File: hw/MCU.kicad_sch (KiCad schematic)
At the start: 14 parts, among them J2 Conn_01x06, SW2 SKRPACE010, SW3 SKRPACE010, U2 N32L406RBL7

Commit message: updated Designs
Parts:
- added C14: 100n, Capacitor_SMD:C_0805_2012Metric_Pad1.18x1.45mm_HandSolder, symbol Device:C
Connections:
- net GND: now also C14.2
- net VDD: now also C14.1
- net HighSide_Row_9: now reaches U2.2 (PC13)
- net HighSide_Row_10: now reaches U2.3 (PC14)
- net HighSide_Row_11: now reaches U2.4 (PC15)
- net HighSide_Row_12: now reaches U2.5 (PD14)
- net HighSide_Input_Row_1 renamed HighSide_Row_1
- net HighSide_Input_Row_2 renamed HighSide_Row_2
- net HighSide_Input_Row_3 renamed HighSide_Row_3
- net HighSide_Input_Row_4 renamed HighSide_Row_4
- net HighSide_Input_Row_5 renamed HighSide_Row_5
- net HighSide_Input_Row_6 renamed HighSide_Row_6
- net HighSide_Input_Row_7 renamed HighSide_Row_7
- net HighSide_Input_Row_8 renamed HighSide_Row_8
- net LowSide_Input_B_Col_1 renamed LowSide_B_Col_1
- net LowSide_Input_B_Col_2 renamed LowSide_B_Col_2
- net LowSide_Input_B_Col_3 renamed LowSide_B_Col_3
- net LowSide_Input_B_Col_4 renamed LowSide_B_Col_4
- net LowSide_Input_B_Col_5 renamed LowSide_B_Col_5
- net LowSide_Input_B_Col_6 renamed LowSide_B_Col_6
- net LowSide_Input_G_Col_1 renamed LowSide_R_Col_2
- net LowSide_Input_G_Col_2 renamed LowSide_G_Col_1
- net LowSide_Input_G_Col_3 renamed LowSide_G_Col_3
- net LowSide_Input_G_Col_4 renamed LowSide_G_Col_4
- net LowSide_Input_G_Col_5 renamed LowSide_G_Col_2
- net LowSide_Input_G_Col_6 renamed LowSide_G_Col_6
- net LowSide_Input_R_Col_1 renamed LowSide_G_Col_5
- net LowSide_Input_R_Col_2 renamed LowSide_R_Col_1
- net LowSide_Input_R_Col_3 renamed LowSide_R_Col_3
- net LowSide_Input_R_Col_4 renamed LowSide_R_Col_4
- net LowSide_Input_R_Col_5 renamed LowSide_R_Col_5
- net LowSide_Input_R_Col_6 renamed LowSide_R_Col_6
- no-connect marks 7 -> 3
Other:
- moved on the sheet: C5, C6, C7, C8

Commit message: routed some row control lines
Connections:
- net LowSide_B_Col_4 is gone; now on net HighSide_Row_6: U2.15 (PA1)
- net LowSide_G_Col_2 is gone; now on net HighSide_Row_3: U2.17 (PA3)
- net LowSide_G_Col_4 is gone; now on net HighSide_Row_9: U2.14 (PA0)
- net LowSide_R_Col_5 is gone; now on net HighSide_Row_4: U2.16 (PA2)
- net HighSide_Row_3: no longer U2.53 (PC12)
- net HighSide_Row_4: no longer U2.54 (PD2)
- net HighSide_Row_6: no longer U2.9 (PC1)
- net HighSide_Row_9: no longer U2.2 (PC13)
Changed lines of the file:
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@@
-    (stroke (width 0) (type default))
-  )
-  (wire (pts (xy 43.18 97.79) (xy 53.34 97.79))
     (stroke (width 0) (type default))
   )
@@
     (stroke (width 0) (type default))
   )
-  (wire (pts (xy 43.18 77.47) (xy 53.34 77.47))
-    (stroke (width 0) (type default))
-  )
   (wire (pts (xy 43.18 58.42) (xy 53.34 58.42))
     (stroke (width 0) (type default))
@@
     (stroke (width 0) (type default))
   )
-  (wire (pts (xy 43.18 105.41) (xy 53.34 105.41))
-    (stroke (width 0) (type default))
-  )
   (wire (pts (xy 168.91 30.48) (xy 168.91 33.02))
     (stroke (width 0) (type default))
@@
   )
   (wire (pts (xy 238.76 88.9) (xy 254 88.9))
-    (stroke (width 0) (type default))
-  )
-  (wire (pts (xy 43.18 100.33) (xy 53.34 100.33))
     (stroke (width 0) (type default))
   )
@@
     (effects (font (size 1.27 1.27)) (justify right bottom))
   )
-  (label "HighSide_Row_9" (at 114.3 81.28 180) (fields_autoplaced)
-    (effects (font (size 1.27 1.27)) (justify right bottom))
-  )
-  (label "LowSide_R_Col_5" (at 114.3 114.3 180) (fields_autoplaced)
+  (label "HighSide_Row_9" (at 114.3 109.22 180) (fields_autoplaced)
     (effects (font (size 1.27 1.27)) (justify right bottom))
   )
@@
     (effects (font (size 1.27 1.27)) (justify right bottom))
   )
-  (label "LowSide_G_Col_4" (at 53.34 97.79 0) (fields_autoplaced)
-    (effects (font (size 1.27 1.27)) (justify left bottom))
-  )
   (label "IMU_INT2" (at 53.34 175.26 0) (fields_autoplaced)
     (effects (font (size 1.27 1.27)) (justify left bottom))
@@
     (effects (font (size 1.27 1.27)) (justify left bottom))
   )
-  (label "LowSide_B_Col_4" (at 53.34 100.33 0) (fields_autoplaced)
-    (effects (font (size 1.27 1.27)) (justify left bottom))
-  )
   (label "HighSide_Row_7" (at 53.34 45.72 0) (fields_autoplaced)
     (effects (font (size 1.27 1.27)) (justify left bottom))
@@
     (effects (font (size 1.27 1.27)) (justify right bottom))
   )
-  (label "LowSide_G_Col_4" (at 114.3 109.22 180) (fields_autoplaced)
-    (effects (font (size 1.27 1.27)) (justify right bottom))
-  )
   (label "LowSide_B_Col_2" (at 160.02 137.16 270) (fields_autoplaced)
     (effects (font (size 1.27 1.27)) (justify right bottom))
@@
     (effects (font (size 1.27 1.27)) (justify right bottom))
   )
-  (label "LowSide_G_Col_2" (at 53.34 77.47 0) (fields_autoplaced)
-    (effects (font (size 1.27 1.27)) (justify left bottom))
-  )
   (label "LowSide_R_Col_1" (at 53.34 64.77 0) (fields_autoplaced)
     (effects (font (size 1.27 1.27)) (justify left bottom))
@@
     (effects (font (size 1.27 1.27)) (justify left bottom))
   )
-  (label "LowSide_R_Col_5" (at 53.34 105.41 0) (fields_autoplaced)
-    (effects (font (size 1.27 1.27)) (justify left bottom))
-  )
   (label "HighSide_Row_11" (at 114.3 86.36 180) (fields_autoplaced)
     (effects (font (size 1.27 1.27)) (justify right bottom))
@@
     (effects (font (size 1.27 1.27)) (justify left bottom))
   )
-  (label "LowSide_G_Col_2" (at 137.16 137.16 270) (fields_autoplaced)
-    (effects (font (size 1.27 1.27)) (justify right bottom))
-  )
   (label "VDDA" (at 175.26 137.16 270) (fields_autoplaced)
     (effects (font (size 1.27 1.27)) (justify right bottom))
@@
     (effects (font (size 1.27 1.27)) (justify right bottom))
   )
-  (label "HighSide_Row_3" (at 162.56 60.96 90) (fields_autoplaced)
-    (effects (font (size 1.27 1.27)) (justify left bottom))
+  (label "HighSide_Row_3" (at 137.16 137.16 270) (fields_autoplaced)
+    (effects (font (size 1.27 1.27)) (justify right bottom))
   )
   (label "LowSide_G_Col_6" (at 53.34 118.11 0) (fields_autoplaced)
     (effects (font (size 1.27 1.27)) (justify left bottom))
   )
-  (label "HighSide_Row_6" (at 114.3 99.06 180) (fields_autoplaced)
+  (label "HighSide_Row_6" (at 114.3 111.76 180) (fields_autoplaced)
     (effects (font (size 1.27 1.27)) (justify right bottom))
   )
@@
     (effects (font (size 1.27 1.27)) (justify left bottom))
   )
-  (label "HighSide_Row_4" (at 160.02 60.96 90) (fields_autoplaced)
-    (effects (font (size 1.27 1.27)) (justify left bottom))
+  (label "HighSide_Row_4" (at 114.3 114.3 180) (fields_autoplaced)
+    (effects (font (size 1.27 1.27)) (justify right bottom))
   )
   (label "IMU_INT2" (at 162.56 137.16 270) (fields_autoplaced)
@@
     (effects (font (size 1.27 1.27)) (justify left bottom))
   )
-  (label "LowSide_B_Col_4" (at 114.3 111.76 180) (fields_autoplaced)
-    (effects (font (size 1.27 1.27)) (justify right bottom))
-  )
   (label "LowSide_B_Col_2" (at 53.34 80.01 0) (fields_autoplaced)
     (effects (font (size 1.27 1.27)) (justify left bottom))
@@
     (effects (font (size 1.27 1.27)) (justify right))
   )
-  (hierarchical_label "LowSide_G_Col_2" (shape output) (at 43.18 77.47 180) (fields_autoplaced)
-    (effects (font (size 1.27 1.27)) (justify right))
-  )
   (hierarchical_label "IMU_MISO" (shape input) (at 43.18 165.1 180) (fields_autoplaced)
     (effects (font (size 1.27 1.27)) (justify right))
@@
     (effects (font (size 1.27 1.27)) (justify right))
   )
-  (hierarchical_label "LowSide_B_Col_4" (shape output) (at 43.18 100.33 180) (fields_autoplaced)
-    (effects (font (size 1.27 1.27)) (justify right))
-  )
   (hierarchical_label "SAO_1_GPIO2" (shape output) (at 43.18 153.67 180) (fields_autoplaced)
     (effects (font (size 1.27 1.27)) (justify right))
   )
-  (hierarchical_label "LowSide_G_Col_4" (shape output) (at 43.18 97.79 180) (fields_autoplaced)
-    (effects (font (size 1.27 1.27)) (justify right))
-  )
   (hierarchical_label "LowSide_R_Col_4" (shape output) (at 43.18 95.25 180) (fields_autoplaced)
-    (effects (font (size 1.27 1.27)) (justify right))
-  )
-  (hierarchical_label "LowSide_R_Col_5" (shape output) (at 43.18 105.41 180) (fields_autoplaced)
     (effects (font (size 1.27 1.27)) (justify right))
   )
@@
     (pin "12")
     (pin "13")
-    (pin "14" (alternate "TIM5_CH1"))
-    (pin "15" (alternate "TIM5_CH2"))
-    (pin "16" (alternate "TIM5_CH3"))
-    (pin "17" (alternate "TIM5_CH4"))
+    (pin "14")
+    (pin "15")
+    (pin "16")
+    (pin "17")
     (pin "18")
     (pin "19")

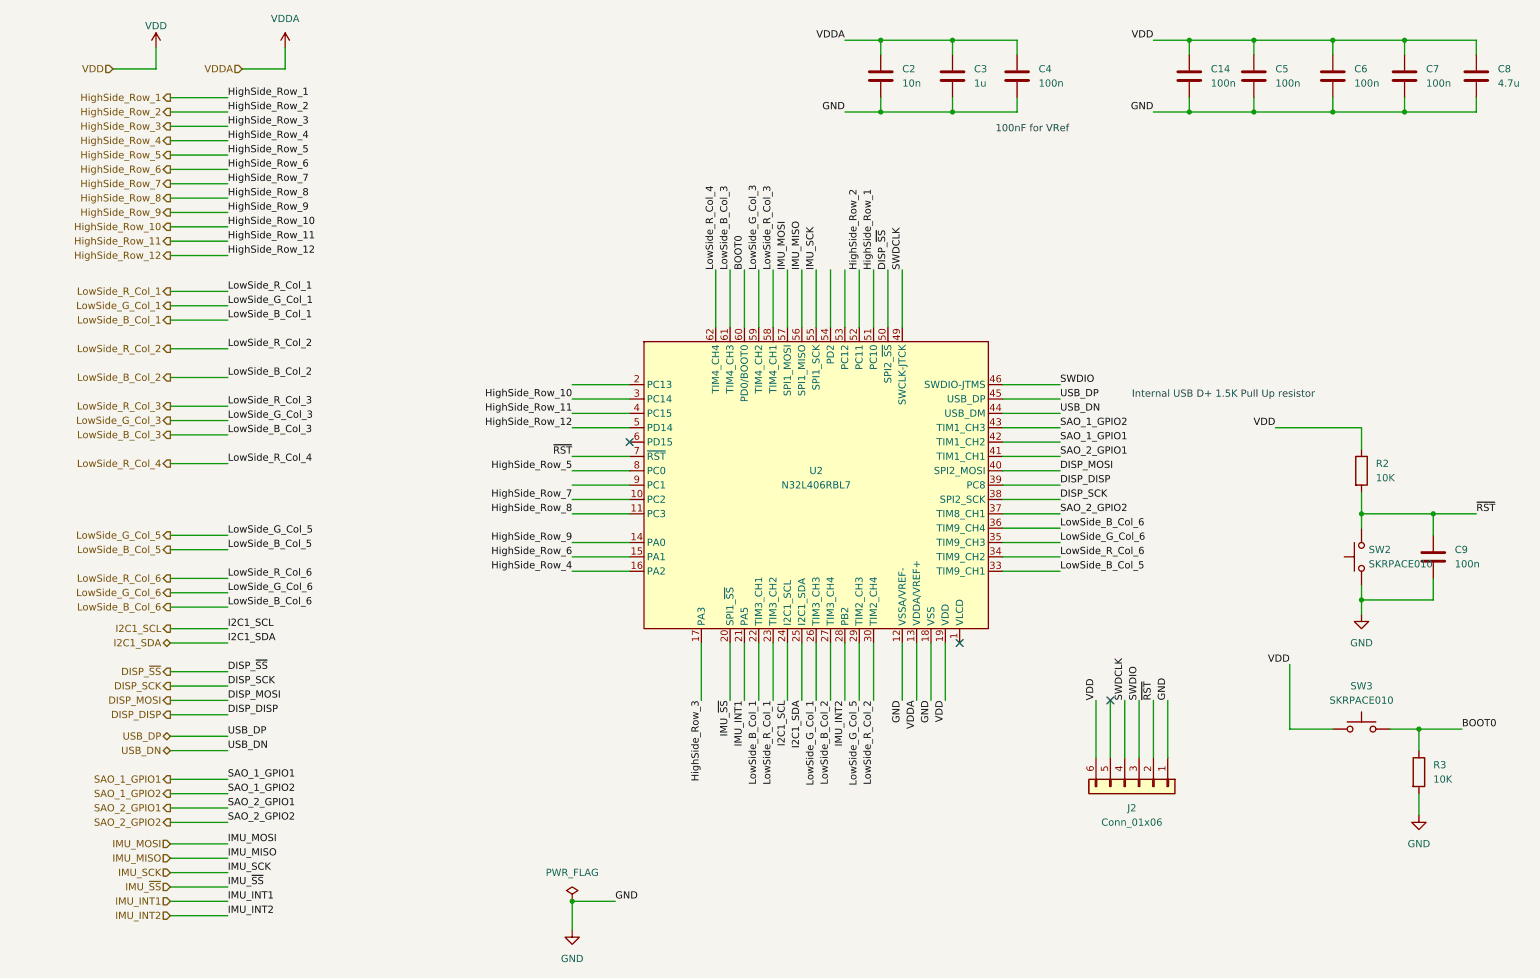
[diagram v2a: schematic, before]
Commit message: routed HighSide MOS
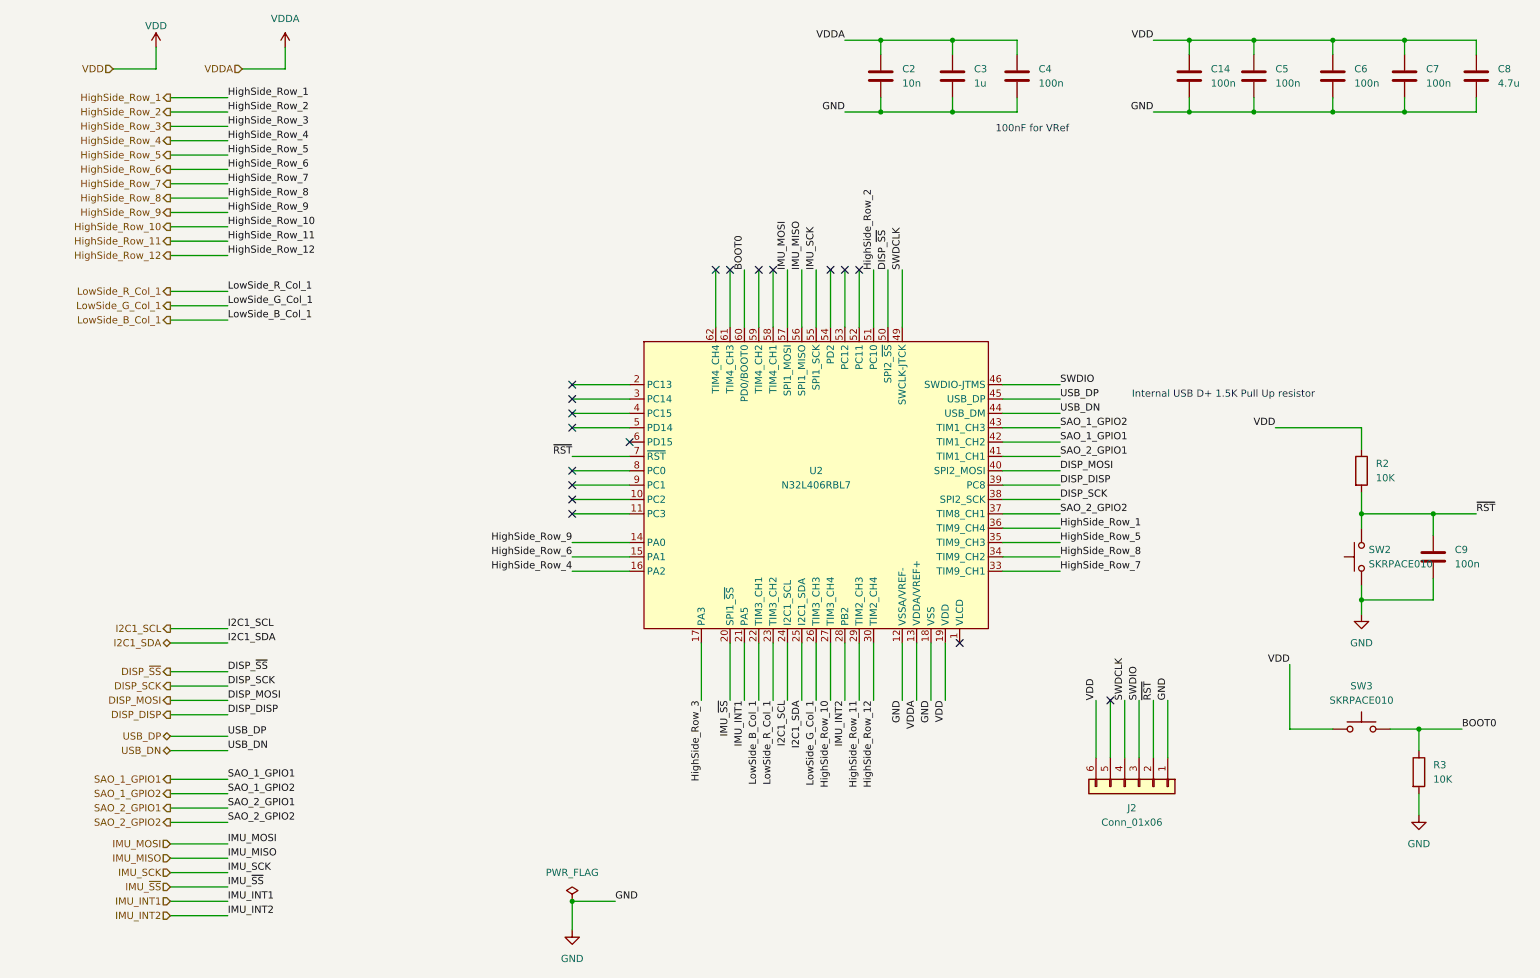
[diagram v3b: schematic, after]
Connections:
- net LowSide_B_Col_2 is gone; now on net HighSide_Row_10: U2.27 (PB1)
- net LowSide_B_Col_5 is gone; now on net HighSide_Row_7: U2.33 (PB12)
- net LowSide_B_Col_6 is gone; now on net HighSide_Row_1: U2.36 (PB15)
- net LowSide_G_Col_5 is gone; now on net HighSide_Row_11: U2.29 (PB10)
- net LowSide_G_Col_6 is gone; now on net HighSide_Row_5: U2.35 (PB14)
- net LowSide_R_Col_2 is gone; now on net HighSide_Row_12: U2.30 (PB11)
- net LowSide_R_Col_6 is gone; now on net HighSide_Row_8: U2.34 (PB13)
- net HighSide_Row_1: no longer U2.51 (PC10)
- net HighSide_Row_10: no longer U2.3 (PC14)
- net HighSide_Row_11: no longer U2.4 (PC15)
- net HighSide_Row_12: no longer U2.5 (PD14)
- net HighSide_Row_2: now also U2.51 (PC10); no longer U2.52 (PC11)
- net HighSide_Row_5: no longer U2.8 (PC0)
- net HighSide_Row_7: no longer U2.10 (PC2)
- net HighSide_Row_8: no longer U2.11 (PC3)
- net LowSide_B_Col_3: no longer names the net of U2.61 (PB8)
- net LowSide_G_Col_3: no longer names the net of U2.59 (PB7)
- net LowSide_R_Col_3: no longer names the net of U2.58 (PB6)
- net LowSide_R_Col_4: no longer names the net of U2.62 (PB9)
- no-connect marks 3 -> 18

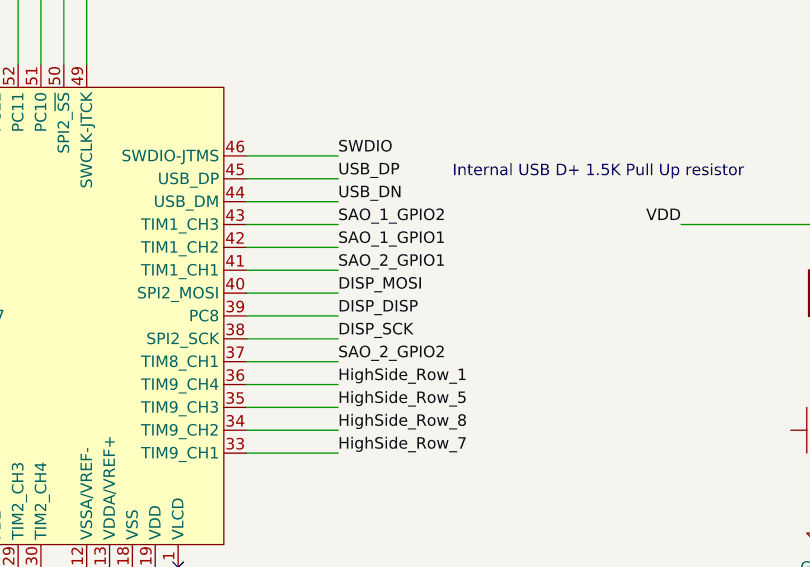
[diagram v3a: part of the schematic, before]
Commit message: routed SAO GPIO
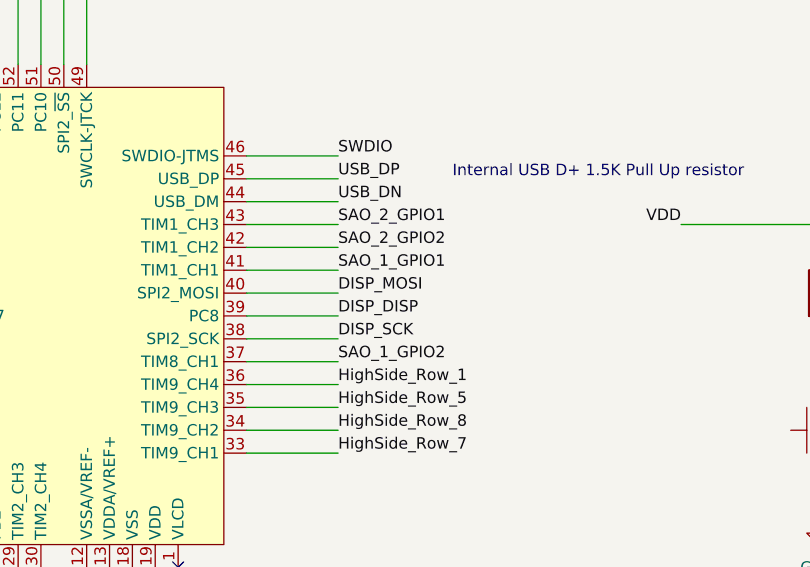
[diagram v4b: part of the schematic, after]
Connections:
- net SAO_1_GPIO1: now also U2.41 (PA8); no longer U2.42 (PA9)
- net SAO_1_GPIO2: now also U2.37 (PC6); no longer U2.43 (PA10)
- net SAO_2_GPIO1: now also U2.43 (PA10); no longer U2.41 (PA8)
- net SAO_2_GPIO2: now also U2.42 (PA9); no longer U2.37 (PC6)
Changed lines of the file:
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@@
     (effects (font (size 1.27 1.27)) (justify left bottom))
   )
-  (label "SAO_2_GPIO2" (at 200.66 104.14 0) (fields_autoplaced)
+  (label "SAO_2_GPIO2" (at 200.66 91.44 0) (fields_autoplaced)
     (effects (font (size 1.27 1.27)) (justify left bottom))
   )
@@
     (effects (font (size 1.27 1.27)) (justify right bottom))
   )
-  (label "SAO_2_GPIO1" (at 200.66 93.98 0) (fields_autoplaced)
+  (label "SAO_2_GPIO1" (at 200.66 88.9 0) (fields_autoplaced)
     (effects (font (size 1.27 1.27)) (justify left bottom))
   )
@@
     (effects (font (size 1.27 1.27)) (justify left bottom))
   )
-  (label "SAO_1_GPIO2" (at 200.66 88.9 0) (fields_autoplaced)
+  (label "SAO_1_GPIO2" (at 200.66 104.14 0) (fields_autoplaced)
     (effects (font (size 1.27 1.27)) (justify left bottom))
   )
@@
     (effects (font (size 1.27 1.27)) (justify left bottom))
   )
-  (label "SAO_1_GPIO1" (at 200.66 91.44 0) (fields_autoplaced)
+  (label "SAO_1_GPIO1" (at 200.66 93.98 0) (fields_autoplaced)
     (effects (font (size 1.27 1.27)) (justify left bottom))
   )
